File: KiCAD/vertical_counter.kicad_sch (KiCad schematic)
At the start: 3 parts, among them U15 74HC161, U16 74HC161, U17 74HC161

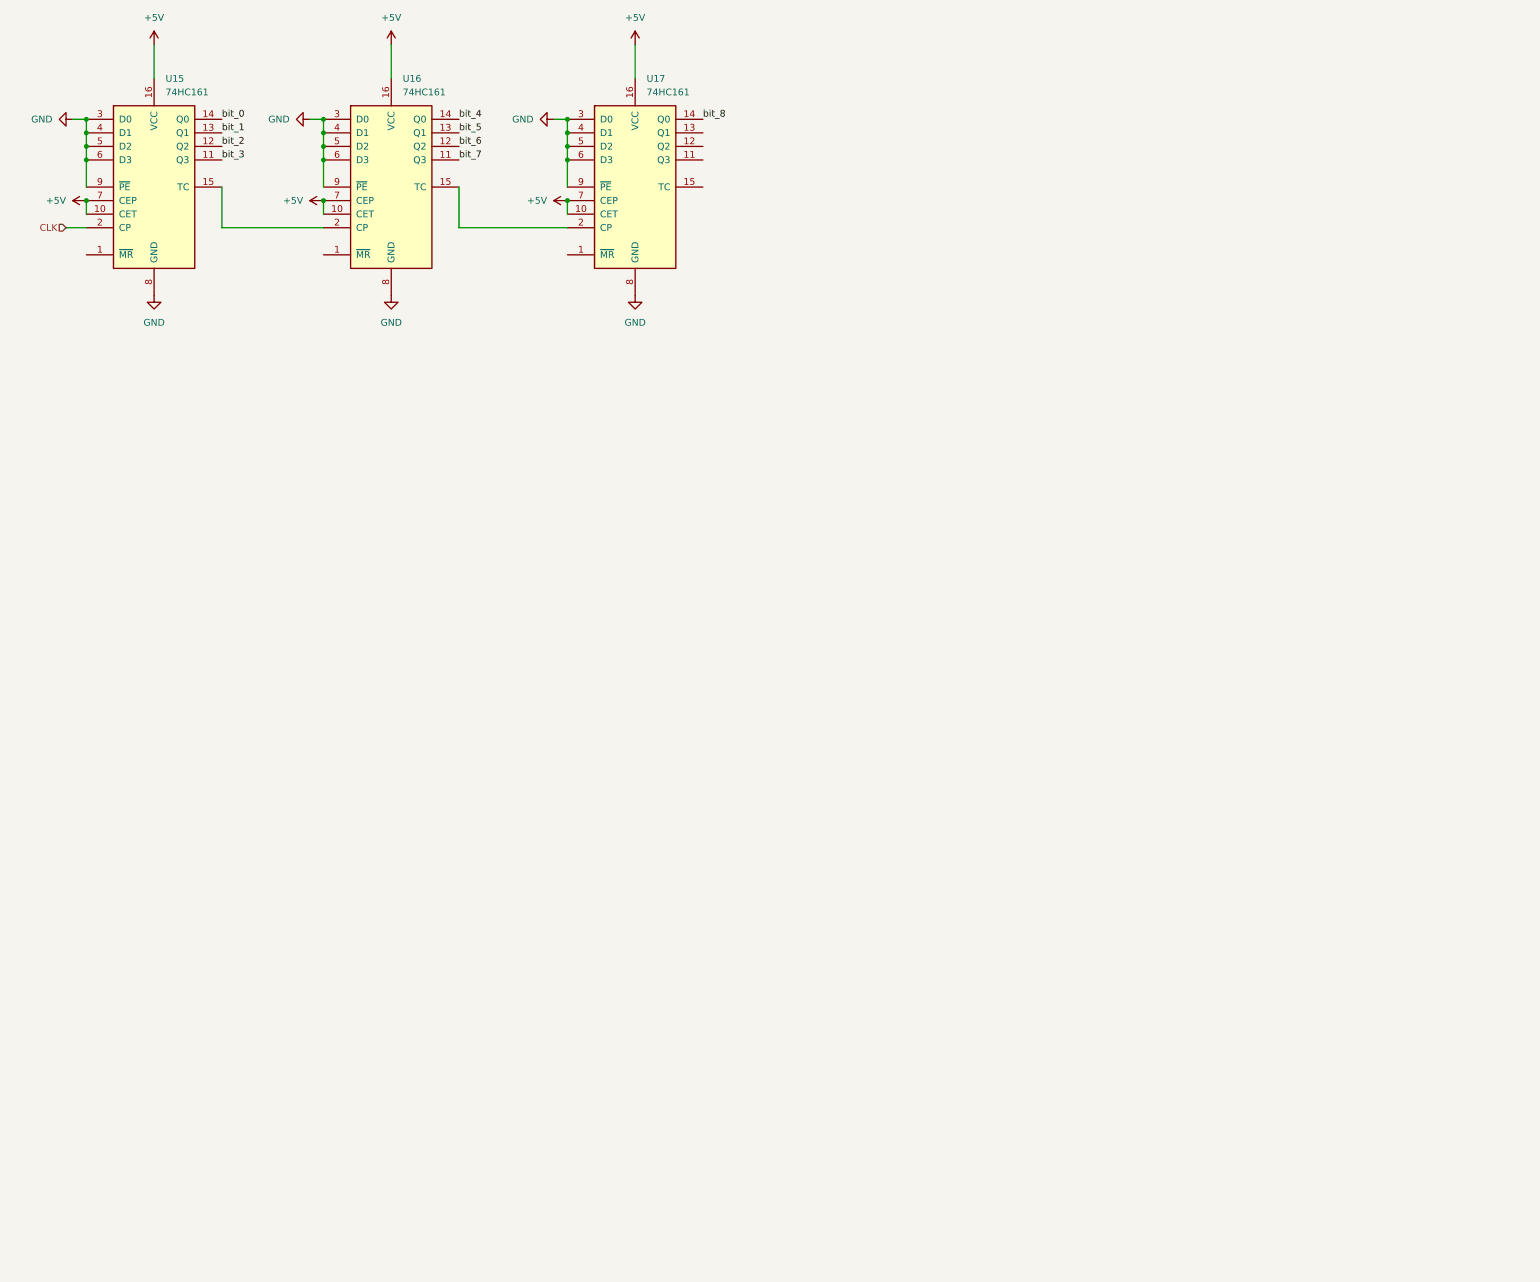
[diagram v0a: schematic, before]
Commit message: assigned footprints
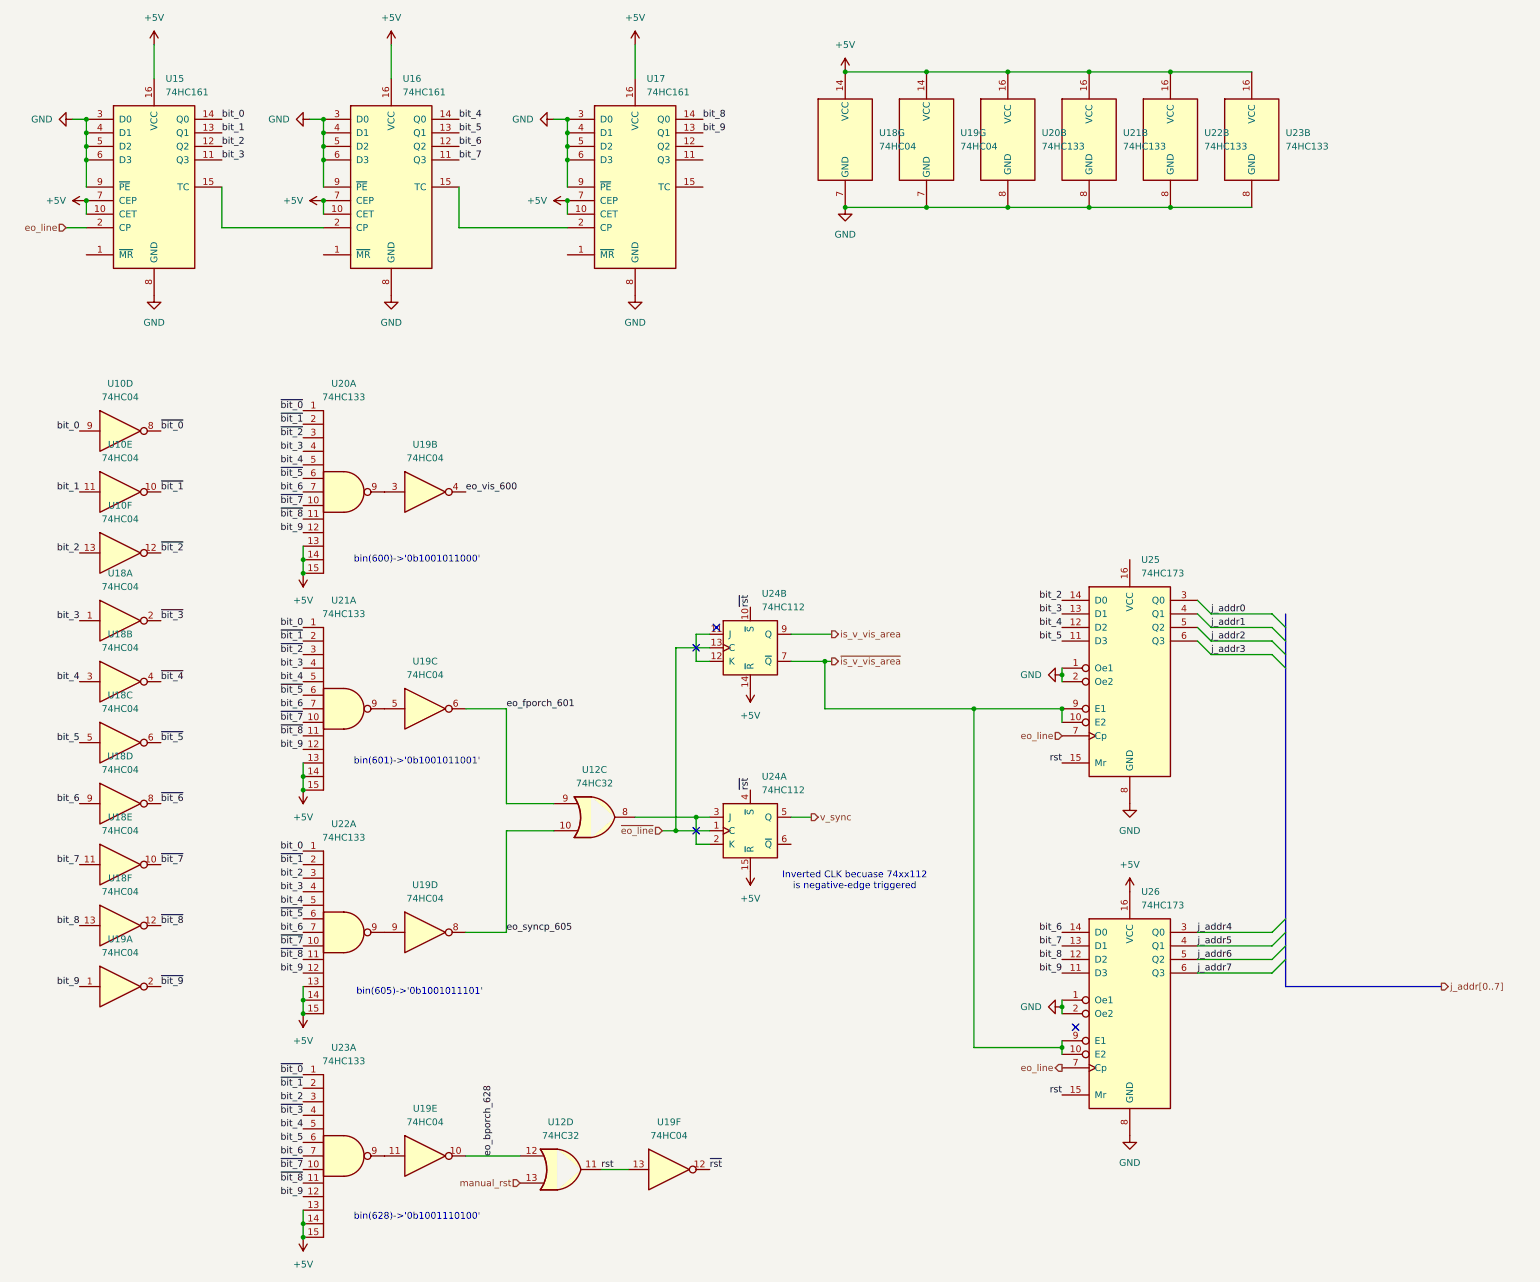
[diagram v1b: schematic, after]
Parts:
- added U10, U18, U19: 74HC04, Package_DIP:DIP-14_W7.62mm, symbol 74xx:74HC04
- added U12: 74HC32, Package_DIP:DIP-14_W7.62mm, symbol 74xx:74LS32
- added U20, U21, U22, U23: 74HC133, Package_DIP:DIP-16_W7.62mm, symbol 74xx:74LS133
- added U24: 74HC112, Package_DIP:DIP-16_W7.62mm, symbol 74xx:74LS112
- added U25, U26: 74HC173, Package_DIP:DIP-16_W7.62mm, symbol 74xx:74HC173
- U15, U16, U17: footprint (none) -> Package_DIP:DIP-16_W7.62mm
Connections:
- net +5V: now also U18.14 (VCC), U19.14 (VCC), U20.13, U20.14, U20.15, U20.16 (VCC), U21.13, U21.14, U21.15, U21.16 (VCC), U22.13, U22.14, U22.15, U22.16 (VCC), U23.13, U23.14, U23.15, U23.16 (VCC), U24.14 (~{R}), U24.15 (~{R}), U26.16 (VCC)
- net GND: now also U18.7 (GND), U19.7 (GND), U20.8 (GND), U21.8 (GND), U22.8 (GND), U23.8 (GND), U25.1 (Oe1), U25.2 (Oe2), U25.8 (GND), U26.1 (Oe1), U26.2 (Oe2), U26.8 (GND)
- net bit_0: now also U10.9, U21.1, U22.1
- net bit_1: now also U10.11
- net bit_2: now also U10.13, U22.3, U23.3, U25.14 (D0)
- net bit_3: now also U18.1, U20.4, U21.4, U22.4, U25.13 (D1)
- net bit_4: now also U18.3, U20.5, U21.5, U22.5, U23.5, U25.12 (D2)
- net bit_5: now also U18.5, U23.6, U25.11 (D3)
- net bit_6: now also U18.9, U20.7, U21.7, U22.7, U23.7, U26.14 (D0)
- net bit_7: now also U18.11, U26.13 (D1)
- net bit_8: now also U18.13, U26.12 (D2)
- net bit_9: now reaches U17.13 (Q1)
- net bit_9: now also U19.1, U20.12, U21.12, U22.12, U23.12, U26.11 (D3)
- net CLK renamed eo_line
- net eo_line: now also U25.7 (Cp), U26.7 (Cp)
- new net: U24.11 (J), U24.12 (K)
- new net: U19.5, U21.9
- new net: U19.11, U23.9
- new net: U12.8, U24.2 (K), U24.3 (J)
- new net: U19.9, U22.9
- new net: U19.3, U20.9
- new net eo_bporch_628: U12.12, U19.10
- new net eo_fporch_601: U12.9, U19.6
- new net eo_syncp_605: U12.10, U19.8
- new net eo_vis_600: U19.4
- new net is_v_vis_area: U24.9 (Q)
- new net j_addr4: U26.3 (Q0)
- new net j_addr5: U26.4 (Q1)
- new net j_addr6: U26.5 (Q2)
- new net j_addr7: U26.6 (Q3)
- new net manual_rst: U12.13
- new net rst: U12.11, U19.13, U25.15 (Mr), U26.15 (Mr)
- new net v_sync: U24.5 (Q)
- new net ~{bit_0}: U10.8, U20.1, U23.1
- new net ~{bit_1}: U10.10, U20.2, U21.2, U22.2, U23.2
- new net ~{bit_2}: U10.12, U20.3, U21.3
- new net ~{bit_3}: U18.2, U23.4
- new net ~{bit_4}: U18.4
- new net ~{bit_5}: U18.6, U20.6, U21.6, U22.6
- new net ~{bit_6}: U18.8
- new net ~{bit_7}: U18.10, U20.10, U21.10, U22.10, U23.10
- new net ~{bit_8}: U18.12, U20.11, U21.11, U22.11, U23.11
- new net ~{bit_9}: U19.2
- new net ~{eo_line}: U24.1 (C), U24.13 (C)
- new net ~{is_v_vis_area}: U24.7 (~{Q}), U25.10 (E2), U25.9 (E1), U26.10 (E2), U26.9 (E1)
- new net ~{rst}: U19.12, U24.10 (~{S}), U24.4 (~{S})
- no-connect marks 0 -> 4
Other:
- note added: "Inverted CLK becuase 74xx112 is negative-edge triggered"
- note added: "bin(600)->'0b1001011000'"
- note added: "bin(601)->'0b1001011001'"
- note added: "bin(605)->'0b1001011101'"
- note added: "bin(628)->'0b1001110100'"
